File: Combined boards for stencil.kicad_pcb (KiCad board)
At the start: 2 copper layers, 180.8 x 95.9 mm, 115 parts, among them J1 RPiZeroW, J2 Iridium, J3 APRS, J4 Antenna, J6 USB_B_Micro, J7 USB, J8 USBPOGO, M1 MountingHole_Pad, M2 MountingHole_Pad, M3 MountingHole_Pad, M4 MountingHole_Pad, M5 PiMount, M6 PiMount, M7 PiMount, M8 PiMount, U1 LSM9DS1BOB, U2 MAX3232, U3 CY7C65213-28PVXI, U3 SC16IS752IPW, Y1 1.8432MHz

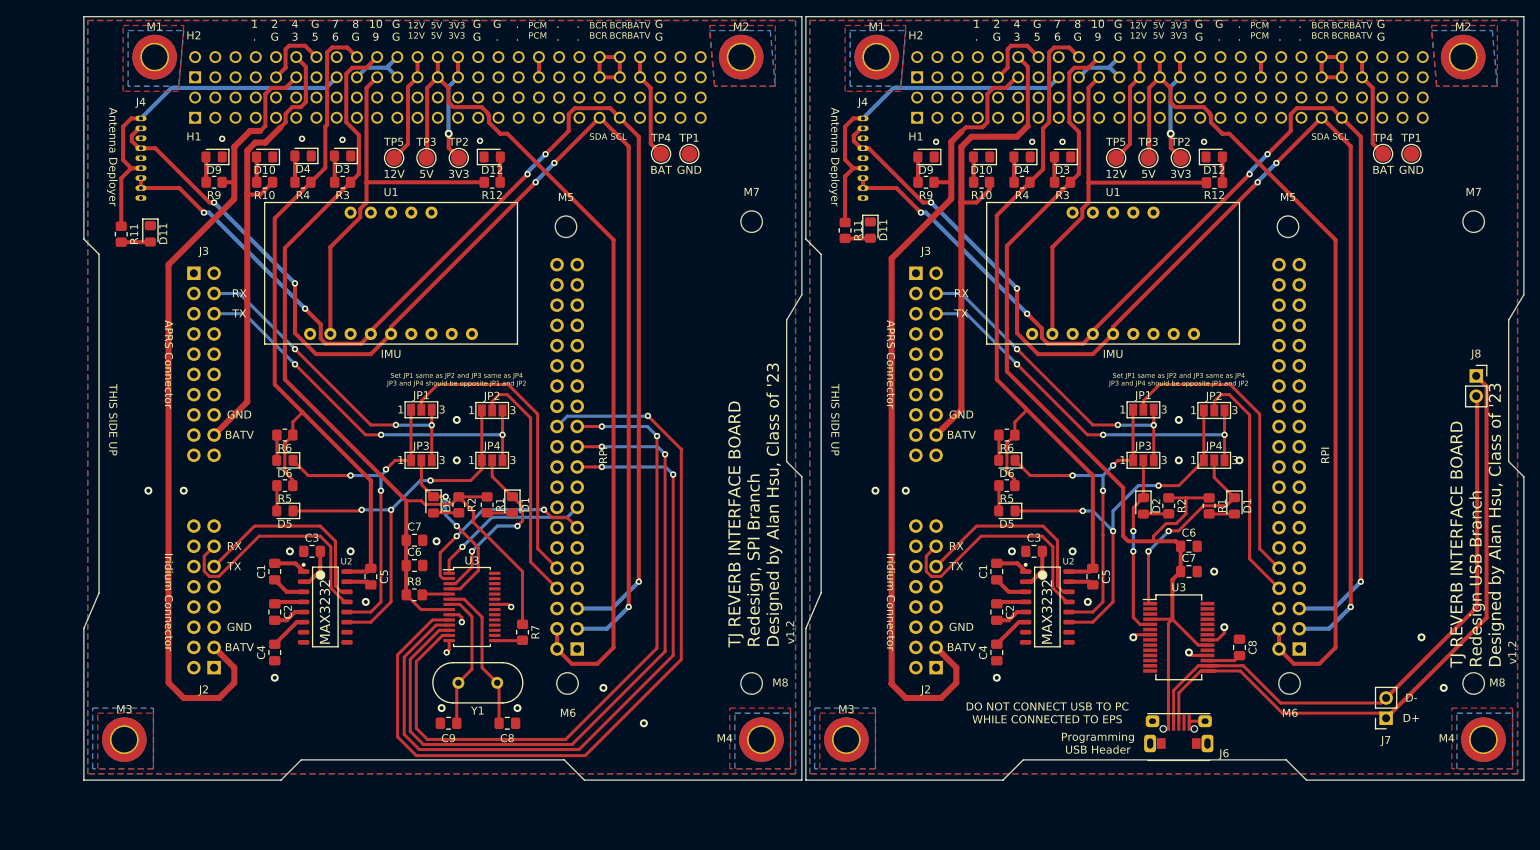
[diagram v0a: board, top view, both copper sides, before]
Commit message: Replace max3232 footprint, update stencil
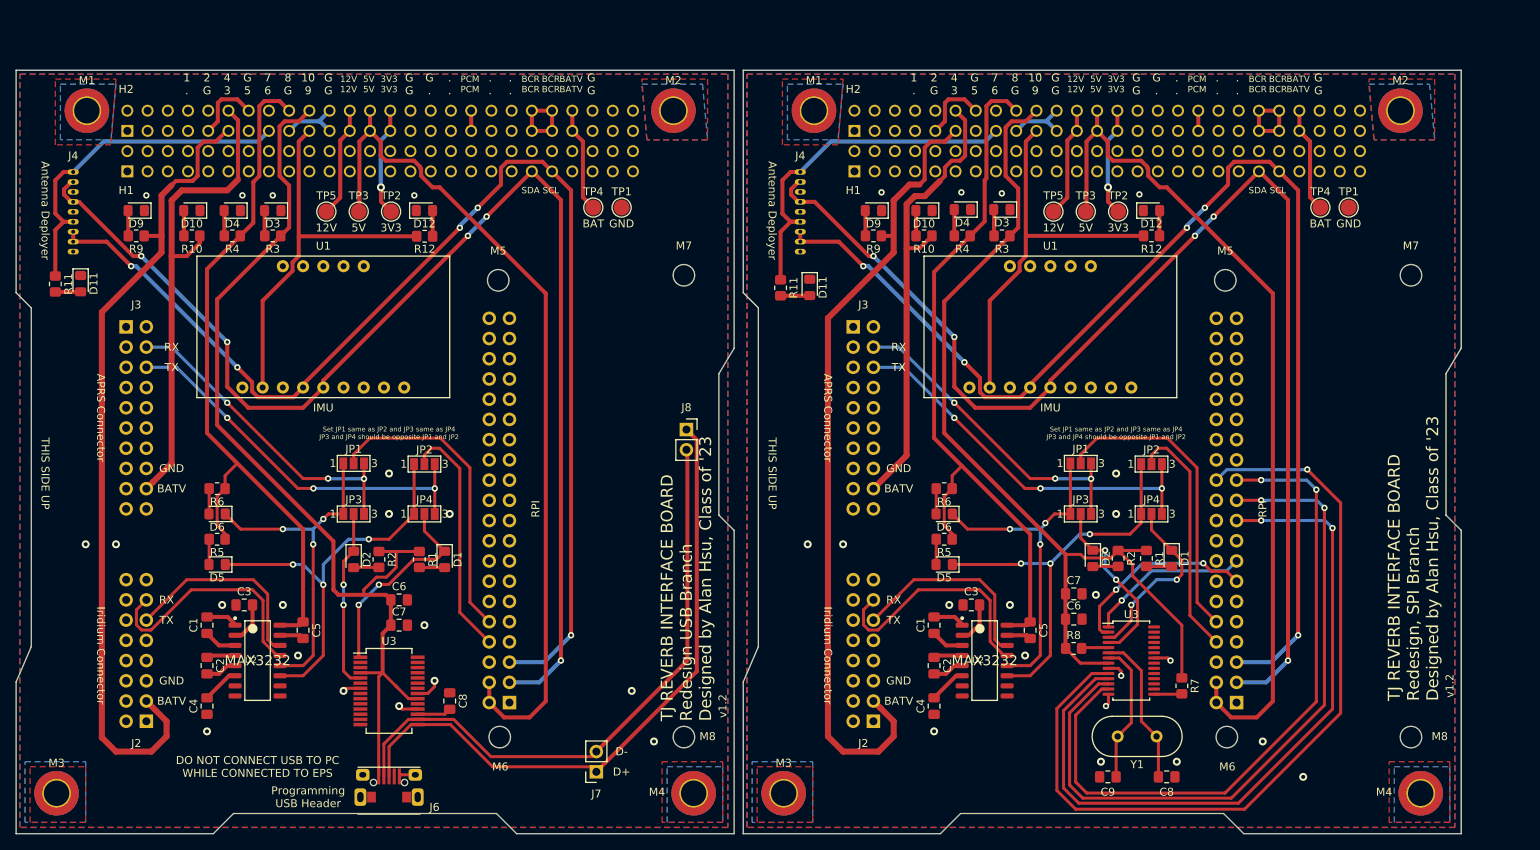
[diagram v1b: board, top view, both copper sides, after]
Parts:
- removed the C1 at (91.4, 125.5)
- removed the C1 at (182.1, 125.5)
- removed the C2 at (91.4, 130.6)
- removed the C2 at (182.1, 130.6)
- removed the C3 at (96.1, 122.9)
- removed the C3 at (186.8, 122.9)
- removed the C4 at (91.4, 135.6)
- removed the C4 at (182.1, 135.6)
- removed the C5 at (103.5, 126.1)
- removed the C5 at (194.2, 126.1)
- removed the D1 at (121.3, 117.1)
- removed the D1 at (212.0, 117.2)
- removed the D2 at (111.4, 117.1)
- removed the D2 at (200.5, 117.2)
- removed the D3 at (99.9, 73.3)
- removed the D3 at (190.4, 73.4)
- removed the D4 at (95.0, 73.3)
- removed the D4 at (185.3, 73.4)
- removed the D5 at (92.7, 117.9)
- removed the D5 at (183.4, 117.9)
- removed the D6 at (92.7, 111.5)
- removed the D6 at (183.4, 111.5)
- removed the H1 at (81.4, 68.5)
- removed the H1 at (172.1, 68.5)
- removed the H2 at (81.4, 63.4)
- removed the H2 at (172.1, 63.4)
- removed the J1 at (129.4, 135.2)
- removed the J1 at (220.1, 135.2)
- removed the J2 at (83.8, 137.5)
- removed the J2 at (174.5, 137.5)
- removed the J3 at (81.3, 88.0)
- removed the J3 at (172.0, 88.0)
- removed the J4 at (74.6, 68.6)
- removed the J4 at (165.3, 68.6)
- removed the JP1 at (109.9, 105.2)
- removed the JP1 at (200.5, 105.2)
- removed the JP2 at (118.7, 105.2)
- removed the JP2 at (209.4, 105.2)
- removed the JP3 at (109.9, 111.5)
- removed the JP3 at (200.5, 111.5)
- removed the JP4 at (118.7, 111.5)
- removed the JP4 at (209.4, 111.5)
- removed the M1 at (76.4, 60.9)
- removed the M1 at (167.0, 60.9)
- removed the M2 at (150.0, 60.9)
- removed the M2 at (240.7, 60.9)
- removed the M3 at (72.5, 146.6)
- removed the M3 at (163.2, 146.6)
- removed the M4 at (152.6, 146.6)
- removed the M4 at (243.2, 146.6)
- removed the M5 at (128.0, 82.2)
- removed the M5 at (218.7, 82.2)
- removed the M6 at (128.2, 139.5)
- removed the M6 at (218.9, 139.5)
- removed the M7 at (151.3, 81.5)
- removed the M7 at (242.0, 81.5)
- removed the M8 at (151.3, 139.5)
- removed the M8 at (242.0, 139.5)
- removed the R1 at (118.1, 117.1)
- removed the R1 at (208.8, 117.2)
- removed the R2 at (114.6, 117.1)
- removed the R2 at (203.7, 117.2)
- removed the R3 at (100.0, 76.6)
- removed the R3 at (190.4, 76.6)
- removed the R4 at (95.0, 76.6)
- removed the R4 at (185.3, 76.6)
- removed the R5 at (92.7, 114.7)
- removed the R5 at (183.4, 114.7)
- removed the R6 at (92.7, 108.3)
- removed the R6 at (183.4, 108.3)
- removed the TP1 at (143.5, 73.0)
- removed the TP1 at (234.2, 73.0)
- removed the TP2 at (114.6, 73.5)
- removed the TP2 at (205.2, 73.5)
- removed the TP3 at (110.5, 73.5)
- removed the TP3 at (201.2, 73.5)
- removed the TP4 at (140.0, 73.0)
- removed the TP4 at (230.6, 73.0)
- removed the TP5 at (106.4, 73.5)
- removed the TP5 at (197.1, 73.5)
- removed the U1 at (106.0, 88.0)
- removed the U1 at (196.7, 88.0)
- removed the U2 at (97.8, 129.9)
- removed the U2 at (188.5, 129.9)
- added C1: 0.1uF, Capacitor_SMD:C_0805_2012Metric_Pad1.18x1.45mm_HandSolder, F.Cu at (82.9, 132.2)
- added C1: 0.1uF, Capacitor_SMD:C_0805_2012Metric_Pad1.18x1.45mm_HandSolder, F.Cu at (174.2, 132.2)
- added C2: 0.47uF, Capacitor_SMD:C_0805_2012Metric_Pad1.18x1.45mm_HandSolder, F.Cu at (82.9, 137.3)
- added C2: 0.47uF, Capacitor_SMD:C_0805_2012Metric_Pad1.18x1.45mm_HandSolder, F.Cu at (174.2, 137.3)
- added C3: 0.47uF, Capacitor_SMD:C_0805_2012Metric_Pad1.18x1.45mm_HandSolder, F.Cu at (87.6, 129.7)
- added C3: 0.47uF, Capacitor_SMD:C_0805_2012Metric_Pad1.18x1.45mm_HandSolder, F.Cu at (178.9, 129.7)
- added C4: 0.47uF, Capacitor_SMD:C_0805_2012Metric_Pad1.18x1.45mm_HandSolder, F.Cu at (82.9, 142.4)
- added C4: 0.47uF, Capacitor_SMD:C_0805_2012Metric_Pad1.18x1.45mm_HandSolder, F.Cu at (174.2, 142.4)
- added C5: 0.1uF, Capacitor_SMD:C_0805_2012Metric_Pad1.18x1.45mm_HandSolder, F.Cu at (95.0, 132.8)
- added C5: 0.1uF, Capacitor_SMD:C_0805_2012Metric_Pad1.18x1.45mm_HandSolder, F.Cu at (186.3, 132.8)
- added D1: RED, LED_SMD:LED_0805_2012Metric_Pad1.15x1.40mm_HandSolder, F.Cu at (112.8, 124.0)
- added D1: RED, LED_SMD:LED_0805_2012Metric_Pad1.15x1.40mm_HandSolder, F.Cu at (204.1, 123.8)
- added D2: GREEN, LED_SMD:LED_0805_2012Metric_Pad1.15x1.40mm_HandSolder, F.Cu at (101.3, 124.0)
- added D2: GREEN, LED_SMD:LED_0805_2012Metric_Pad1.15x1.40mm_HandSolder, F.Cu at (194.2, 123.8)
- added D3: RED, LED_SMD:LED_0805_2012Metric_Pad1.15x1.40mm_HandSolder, F.Cu at (91.2, 80.1)
- added D3: RED, LED_SMD:LED_0805_2012Metric_Pad1.15x1.40mm_HandSolder, F.Cu at (182.8, 80.0)
- added D4: RED, LED_SMD:LED_0805_2012Metric_Pad1.15x1.40mm_HandSolder, F.Cu at (86.1, 80.1)
- added D4: RED, LED_SMD:LED_0805_2012Metric_Pad1.15x1.40mm_HandSolder, F.Cu at (177.8, 80.0)
- added D5: RED, LED_SMD:LED_0805_2012Metric_Pad1.15x1.40mm_HandSolder, F.Cu at (84.2, 124.6)
- added D5: RED, LED_SMD:LED_0805_2012Metric_Pad1.15x1.40mm_HandSolder, F.Cu at (175.5, 124.6)
- added D6: GREEN, LED_SMD:LED_0805_2012Metric_Pad1.15x1.40mm_HandSolder, F.Cu at (84.2, 118.2)
- added D6: GREEN, LED_SMD:LED_0805_2012Metric_Pad1.15x1.40mm_HandSolder, F.Cu at (175.5, 118.2)
- added H1: EPS Stack Header 2, REVERB Interface:PinSocket_2x26_P2.54mm_Vertical, B.Cu at (72.9, 75.2)
- added H1: EPS Stack Header 2, REVERB Interface:PinSocket_2x26_P2.54mm_Vertical, B.Cu at (164.2, 75.2)
- added H2: EPS Stack Header 1, REVERB Interface:PinSocket_2x26_P2.54mm_Vertical, B.Cu at (72.9, 70.1)
- added H2: EPS Stack Header 1, REVERB Interface:PinSocket_2x26_P2.54mm_Vertical, B.Cu at (164.2, 70.1)
- added J1: RPiZeroW, Connector_PinSocket_2.54mm:PinSocket_2x20_P2.54mm_Vertical, B.Cu at (120.9, 141.9)
- added J1: RPiZeroW, Connector_PinSocket_2.54mm:PinSocket_2x20_P2.54mm_Vertical, B.Cu at (212.2, 141.9)
- added J2: Iridium, Connector_PinSocket_2.54mm:PinSocket_2x08_P2.54mm_Vertical, B.Cu at (75.3, 144.3)
- added J2: Iridium, Connector_PinSocket_2.54mm:PinSocket_2x08_P2.54mm_Vertical, B.Cu at (166.6, 144.3)
- added J3: APRS, Connector_PinSocket_2.54mm:PinSocket_2x10_P2.54mm_Vertical, B.Cu at (72.8, 94.7)
- added J3: APRS, Connector_PinSocket_2.54mm:PinSocket_2x10_P2.54mm_Vertical, B.Cu at (164.1, 94.7)
- added J4: Antenna, REVERB Interface:1.25mmPitchHeader, F.Cu at (66.1, 75.3)
- added J4: Antenna, REVERB Interface:1.25mmPitchHeader, F.Cu at (157.4, 75.3)
- added JP1: HWRX, Jumper:SolderJumper-3_P1.3mm_Open_Pad1.0x1.5mm_NumberLabels, F.Cu at (101.3, 111.9)
- added JP1: HWRX, Jumper:SolderJumper-3_P1.3mm_Open_Pad1.0x1.5mm_NumberLabels, F.Cu at (192.7, 111.9)
- added JP2: HWTX, Jumper:SolderJumper-3_P1.3mm_Open_Pad1.0x1.5mm_NumberLabels, F.Cu at (110.2, 112.0)
- added JP2: HWTX, Jumper:SolderJumper-3_P1.3mm_Open_Pad1.0x1.5mm_NumberLabels, F.Cu at (201.5, 112.0)
- added JP3: USBUARTRX, Jumper:SolderJumper-3_P1.3mm_Open_Pad1.0x1.5mm_NumberLabels, F.Cu at (101.3, 118.2)
- added JP3: SPIUARTRX, Jumper:SolderJumper-3_P1.3mm_Open_Pad1.0x1.5mm_NumberLabels, F.Cu at (192.7, 118.2)
- added JP4: USBUARTTX, Jumper:SolderJumper-3_P1.3mm_Open_Pad1.0x1.5mm_NumberLabels, F.Cu at (110.2, 118.2)
- added JP4: SPIUARTTX, Jumper:SolderJumper-3_P1.3mm_Open_Pad1.0x1.5mm_NumberLabels, F.Cu at (201.5, 118.2)
- added M1: MountingHole_Pad, MountingHole:MountingHole_3.2mm_M3_DIN965_Pad_TopBottom, F.Cu at (67.8, 67.6)
- added M1: MountingHole_Pad, MountingHole:MountingHole_3.2mm_M3_DIN965_Pad_TopBottom, F.Cu at (159.2, 67.6)
- added M2: MountingHole_Pad, MountingHole:MountingHole_3.2mm_M3_DIN965_Pad_TopBottom, F.Cu at (141.5, 67.6)
- added M2: MountingHole_Pad, MountingHole:MountingHole_3.2mm_M3_DIN965_Pad_TopBottom, F.Cu at (232.8, 67.6)
- added M3: MountingHole_Pad, MountingHole:MountingHole_3.2mm_M3_DIN965_Pad_TopBottom, F.Cu at (64.0, 153.3)
- added M3: MountingHole_Pad, MountingHole:MountingHole_3.2mm_M3_DIN965_Pad_TopBottom, F.Cu at (155.3, 153.3)
- added M4: MountingHole_Pad, MountingHole:MountingHole_3.2mm_M3_DIN965_Pad_TopBottom, F.Cu at (144.0, 153.3)
- added M4: MountingHole_Pad, MountingHole:MountingHole_3.2mm_M3_DIN965_Pad_TopBottom, F.Cu at (235.4, 153.3)
- added M5: PiMount, MountingHole:MountingHole_2.7mm_M2.5, F.Cu at (119.5, 88.9)
- added M5: PiMount, MountingHole:MountingHole_2.7mm_M2.5, F.Cu at (210.8, 88.9)
- added M6: PiMount, MountingHole:MountingHole_2.7mm_M2.5, F.Cu at (119.7, 146.3)
- added M6: PiMount, MountingHole:MountingHole_2.7mm_M2.5, F.Cu at (211.0, 146.3)
- added M7: PiMount, MountingHole:MountingHole_2.7mm_M2.5, F.Cu at (142.8, 88.3)
- added M7: PiMount, MountingHole:MountingHole_2.7mm_M2.5, F.Cu at (234.1, 88.3)
- added M8: PiMount, MountingHole:MountingHole_2.7mm_M2.5, F.Cu at (142.8, 146.3)
- added M8: PiMount, MountingHole:MountingHole_2.7mm_M2.5, F.Cu at (234.1, 146.3)
- added R1: 1K, Resistor_SMD:R_0805_2012Metric_Pad1.20x1.40mm_HandSolder, F.Cu at (109.6, 124.0)
- added R1: 1K, Resistor_SMD:R_0805_2012Metric_Pad1.20x1.40mm_HandSolder, F.Cu at (200.9, 123.8)
- added R2: 1K, Resistor_SMD:R_0805_2012Metric_Pad1.20x1.40mm_HandSolder, F.Cu at (104.5, 124.0)
- added R2: 1K, Resistor_SMD:R_0805_2012Metric_Pad1.20x1.40mm_HandSolder, F.Cu at (197.4, 123.8)
- added R3: 1K, Resistor_SMD:R_0805_2012Metric_Pad1.20x1.40mm_HandSolder, F.Cu at (91.2, 83.3)
- added R3: 1K, Resistor_SMD:R_0805_2012Metric_Pad1.20x1.40mm_HandSolder, F.Cu at (182.8, 83.3)
- added R4: 1K, Resistor_SMD:R_0805_2012Metric_Pad1.20x1.40mm_HandSolder, F.Cu at (86.1, 83.3)
- added R4: 1K, Resistor_SMD:R_0805_2012Metric_Pad1.20x1.40mm_HandSolder, F.Cu at (177.8, 83.3)
- added R5: 1K, Resistor_SMD:R_0805_2012Metric_Pad1.20x1.40mm_HandSolder, F.Cu at (84.2, 121.4)
- added R5: 1K, Resistor_SMD:R_0805_2012Metric_Pad1.20x1.40mm_HandSolder, F.Cu at (175.5, 121.4)
- added R6: 1K, Resistor_SMD:R_0805_2012Metric_Pad1.20x1.40mm_HandSolder, F.Cu at (84.2, 115.1)
- added R6: 1K, Resistor_SMD:R_0805_2012Metric_Pad1.20x1.40mm_HandSolder, F.Cu at (175.5, 115.1)
- added TP1: GND, TestPoint:TestPoint_Pad_D2.0mm, F.Cu at (135.0, 79.8)
- added TP1: GND, TestPoint:TestPoint_Pad_D2.0mm, F.Cu at (226.3, 79.8)
- added TP2: 3V3, TestPoint:TestPoint_Pad_D2.0mm, F.Cu at (106.0, 80.3)
- added TP2: 3V3, TestPoint:TestPoint_Pad_D2.0mm, F.Cu at (197.4, 80.3)
- added TP3: 5V, TestPoint:TestPoint_Pad_D2.0mm, F.Cu at (102.0, 80.3)
- added TP3: 5V, TestPoint:TestPoint_Pad_D2.0mm, F.Cu at (193.3, 80.3)
- added TP4: BAT, TestPoint:TestPoint_Pad_D2.0mm, F.Cu at (131.4, 79.8)
- added TP4: BAT, TestPoint:TestPoint_Pad_D2.0mm, F.Cu at (222.8, 79.8)
- added TP5: 12V, TestPoint:TestPoint_Pad_D2.0mm, F.Cu at (97.9, 80.3)
- added TP5: 12V, TestPoint:TestPoint_Pad_D2.0mm, F.Cu at (189.2, 80.3)
- added U1: LSM9DS1BOB, REVERB Interface:LSM9DS1BOB, F.Cu at (97.5, 94.7)
- added U1: LSM9DS1BOB, REVERB Interface:LSM9DS1BOB, F.Cu at (188.8, 94.7)
- added U2: MAX3232, REVERB Interface:Texas_Instruments-MAX3232ID-Level_A, F.Cu at (89.3, 136.7)
- added U2: MAX3232, REVERB Interface:Texas_Instruments-MAX3232ID-Level_A, F.Cu at (180.6, 136.7)
- moved C8 99.4 mm to (113.4, 141.7)
- moved D9 99.4 mm to (74.0, 80.1)
- moved J6 99.4 mm to (105.8, 153.8)
- moved J7 99.4 mm to (131.8, 150.6)
- moved J8 99.4 mm to (143.1, 107.6)
- moved R11 99.4 mm to (63.9, 89.4)
- moved R9 99.4 mm to (74.0, 83.3)
- moved U3 99.4 mm to (105.8, 140.5)
- moved D10 99.4 mm to (81.0, 80.1)
- moved D11 99.4 mm to (67.1, 89.3)
- moved D12 99.4 mm to (110.2, 80.1)
- moved R10 99.4 mm to (81.0, 83.3)
- moved R12 99.4 mm to (110.3, 83.4)
- moved C6 99.4 mm to (107.1, 129.0)
- moved C7 99.4 mm to (107.1, 132.2)
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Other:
- board size 180.8 x 95.9 mm -> 181.5 x 95.9 mm
